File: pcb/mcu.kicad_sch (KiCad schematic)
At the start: 16 parts, among them J302 JTAG, J501 UART, SW501 Reset, SW502 Boot, U501 ESP32-S3-WROOM-1

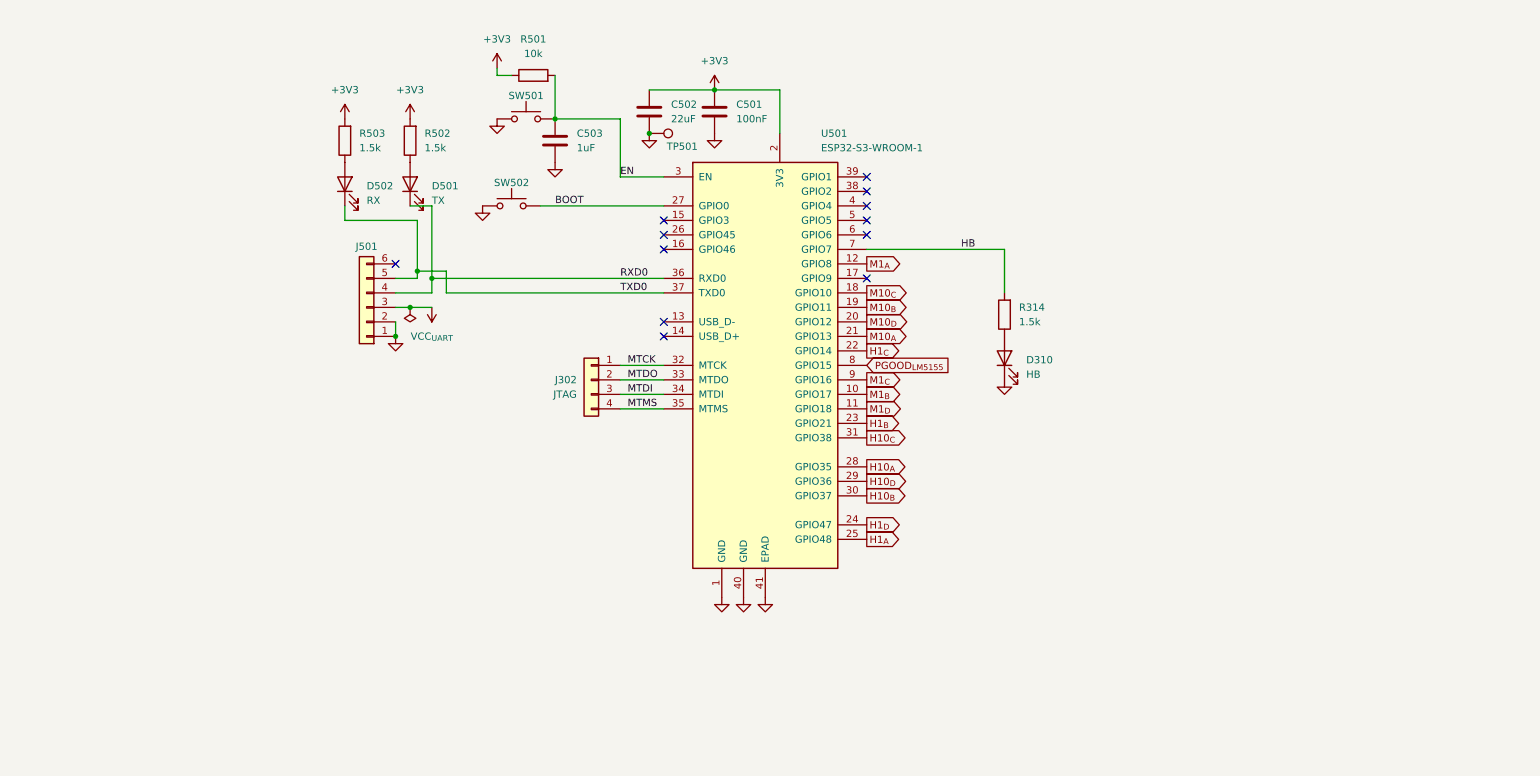
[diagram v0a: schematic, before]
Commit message: Partial Rev B, committing before splitting projects
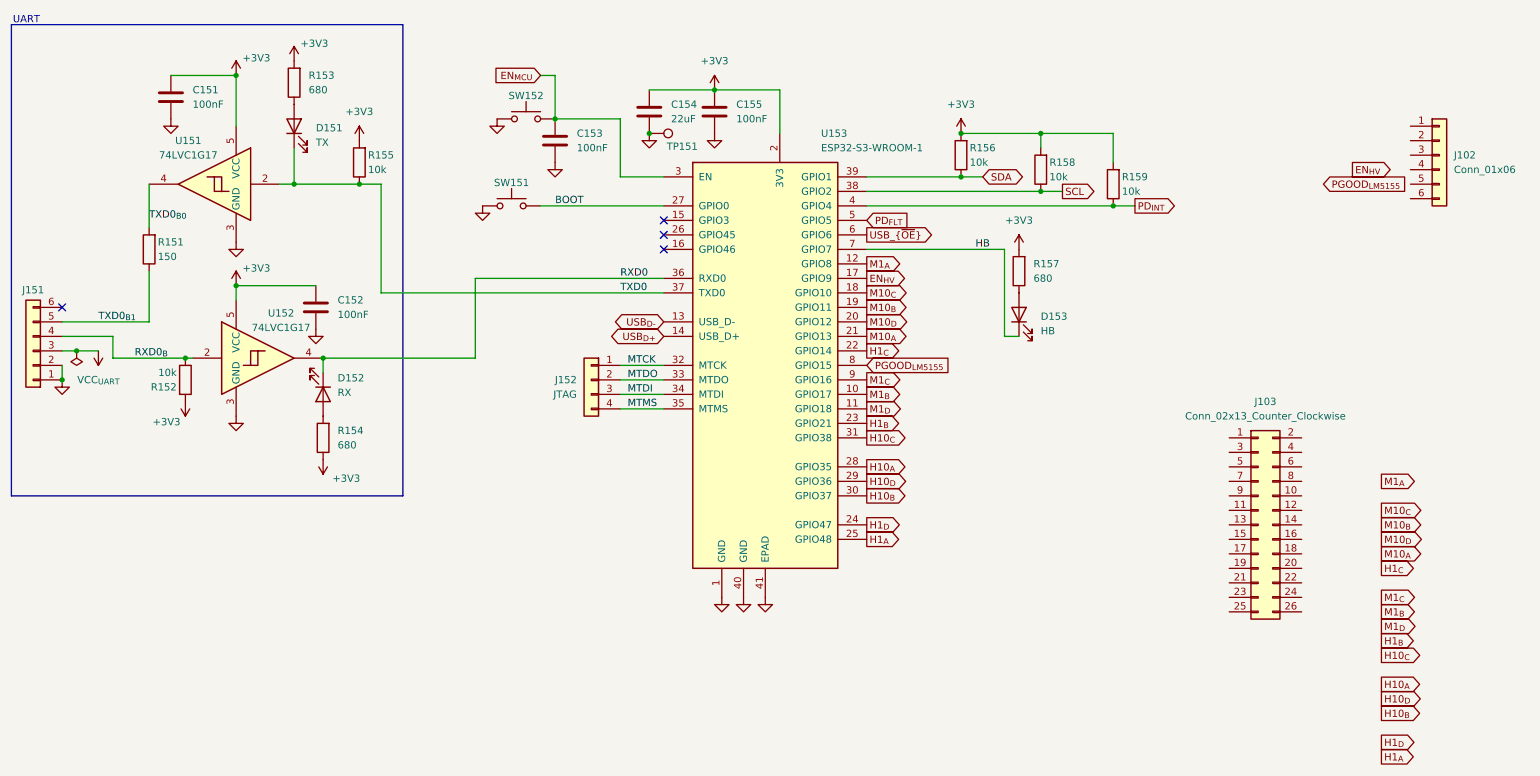
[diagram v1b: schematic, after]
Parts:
- removed C503: 1uF, Capacitor_SMD:C_0805_2012Metric_Pad1.18x1.45mm_HandSolder, symbol Device:C
- removed D310: HB, LED_SMD:LED_0805_2012Metric_Pad1.15x1.40mm_HandSolder, symbol Device:LED
- removed D501: TX, LED_SMD:LED_0805_2012Metric_Pad1.15x1.40mm_HandSolder, symbol Device:LED
- removed D502: RX, LED_SMD:LED_0805_2012Metric_Pad1.15x1.40mm_HandSolder, symbol Device:LED
- removed R314, R502, R503: 1.5k, Resistor_SMD:R_0805_2012Metric_Pad1.20x1.40mm_HandSolder, symbol Device:R
- removed R501: 10k, Resistor_SMD:R_0805_2012Metric_Pad1.20x1.40mm_HandSolder, symbol Device:R
- added C151, C152, C153: 100nF, Capacitor_SMD:C_0402_1005Metric, symbol Device:C
- added D151: TX, LED_SMD:LED_0603_1608Metric, symbol Device:LED
- added D152: RX, LED_SMD:LED_0603_1608Metric, symbol Device:LED
- added D153: HB, LED_SMD:LED_0603_1608Metric, symbol Device:LED
- added J102: Conn_01x06, Connector_JST:JST_XH_S6B-XH-A_1x06_P2.50mm_Horizontal, symbol Connector_Generic:Conn_01x06
- added J103: Conn_02x13_Counter_Clockwise, Connector_IDC:IDC-Header_2x13_P2.54mm_Vertical, symbol Connector_Generic:Conn_02x13_Odd_Even
- added R151: 150, Resistor_SMD:R_0402_1005Metric, symbol Device:R
- added R152, R155, R156, R158, R159: 10k, Resistor_SMD:R_0402_1005Metric, symbol Device:R
- added R153, R154, R157: 680, Resistor_SMD:R_0402_1005Metric, symbol Device:R
- added U151, U152: 74LVC1G17, Package_TO_SOT_SMD:SOT-23-5, symbol 74xGxx:74LVC1G17
- C154: renamed from C502; footprint Capacitor_SMD:C_0805_2012Metric_Pad1.18x1.45mm_HandSolder -> Capacitor_SMD:C_0603_1608Metric; LCSC (none) -> C59461; MFG Part No GMC21X5R226M25NT -> CL10A226MQ8NRNC
- C155: renamed from C501; footprint Capacitor_SMD:C_0805_2012Metric_Pad1.18x1.45mm_HandSolder -> Capacitor_SMD:C_0402_1005Metric; LCSC (none) -> C1525; MFG Part No C0805C104K3RACTU -> CL05B104KO5NNNC
- renumbered J501 to J151, J302 to J152, SW502 to SW151, SW501 to SW152, TP501 to TP151, U501 to U153
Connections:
- net +3V3: now also C151.1, C152.1, R152.2, R153.2, R154.1, R155.2, R156.2, R157.2, R158.2, R159.2, U151.5 (VCC), U152.5 (VCC)
- net GND: now also C151.2, C152.2, C153.2, U151.3 (GND), U152.3 (GND)
- net HB: now also D153.1 (K)
- net RXD0: now also D152.1 (K), U152.4; no longer J151.4 (Pin_4)
- net TXD0: now also D151.1 (K), R155.1, U151.2; no longer J151.5 (Pin_5)
- net USB_{D-}: now reaches U153.13 (USB_D-)
- net USB_{D+}: now reaches U153.14 (USB_D+)
- net EN_{HV}: now reaches U153.17 (GPIO9)
- net SCL: now reaches U153.38 (GPIO2)
- net SCL: now also R158.1
- net SDA: now reaches U153.39 (GPIO1)
- net SDA: now also R156.1
- net PD_{INT}: now reaches U153.4 (GPIO4)
- net PD_{INT}: now also R159.1
- net PD_{FLT}: now reaches U153.5 (GPIO5)
- net USB_{~{OE}}: now reaches U153.6 (GPIO6)
- net EN renamed EN_{MCU}
- net EN_{MCU}: now also C153.1
- new net: D151.2 (A), R153.1
- new net: D153.2 (A), R157.1
- new net: D152.2 (A), R154.2
- new net RXD0_{B}: J151.4 (Pin_4), R152.1, U152.2
- new net TXD0_{B0}: R151.2, U151.4
- new net TXD0_{B1}: J151.5 (Pin_5), R151.1
- no-connect marks 12 -> 4
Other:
- note added: "UART"
- moved on the sheet: J151
